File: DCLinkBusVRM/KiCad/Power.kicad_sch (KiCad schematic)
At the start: 34 parts

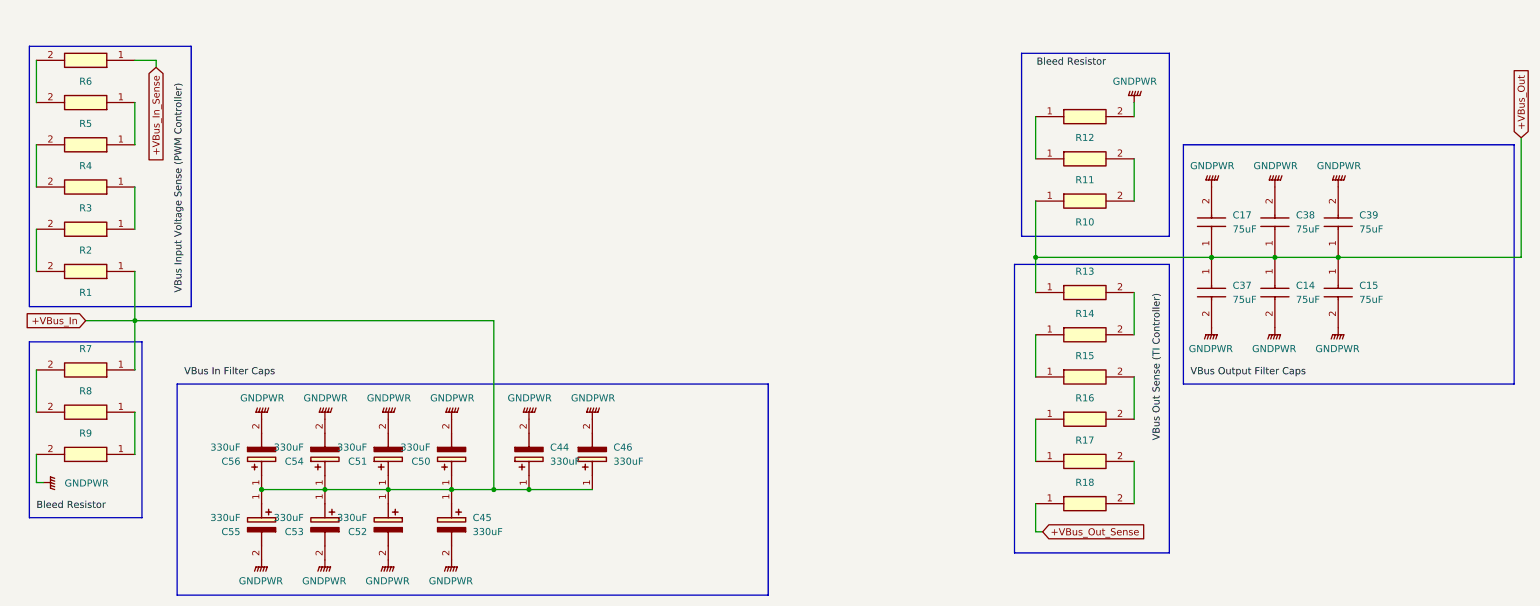
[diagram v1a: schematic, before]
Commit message: Update Canbus protocol for vrm
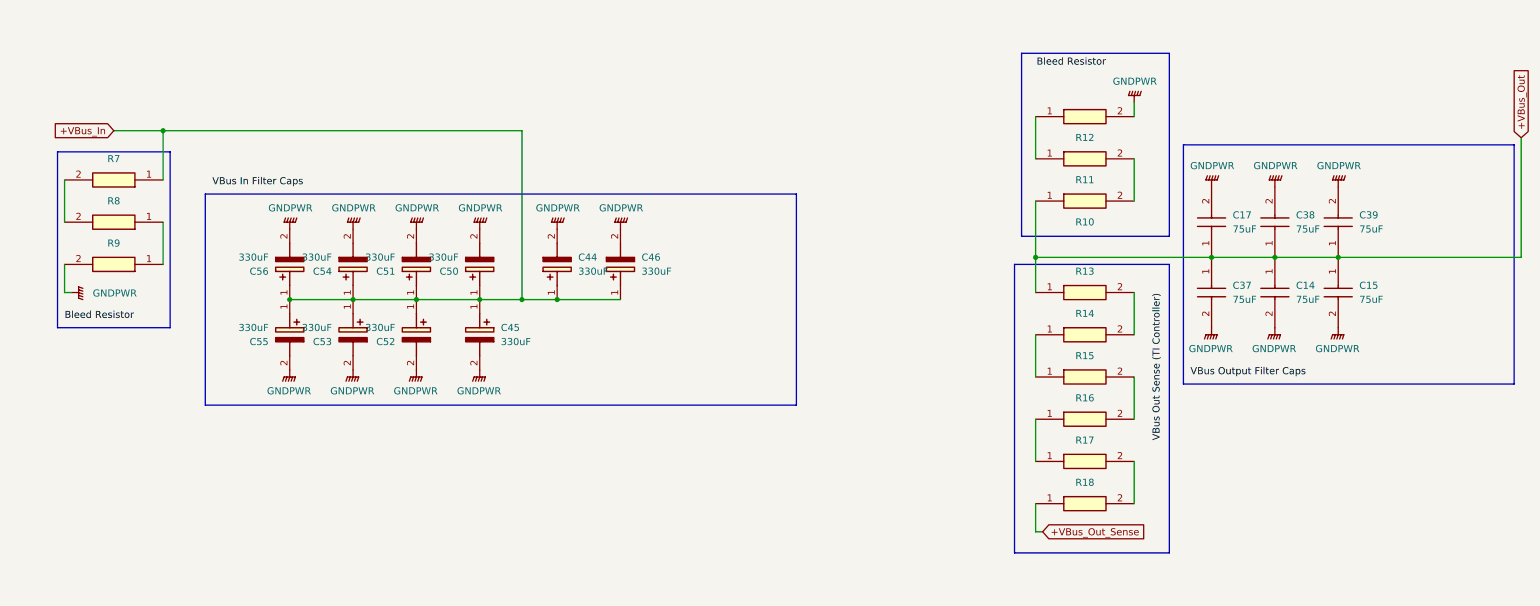
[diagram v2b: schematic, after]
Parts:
- removed R1, R2, R3, R4, R5, R6: RC2512JK-071ML, InverterCom:RESC6431X65N, symbol InverterCom:RC2512JK-071ML
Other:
- moved on the sheet: C44, C45, C46, C50, C51, C52, C53, C54, C55, C56, R7, R8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
